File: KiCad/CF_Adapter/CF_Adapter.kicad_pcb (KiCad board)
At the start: 2 copper layers, 38.1 x 53.3 mm, 3 parts, among them J1 Z-Fighter IDE Connector, J2 CF Card Socket

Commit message: Silkscreen, Gerber settings
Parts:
- added G***: LOGO, Z-Fighter:Tangent_Head, B.Cu at (150.9, 117.5)

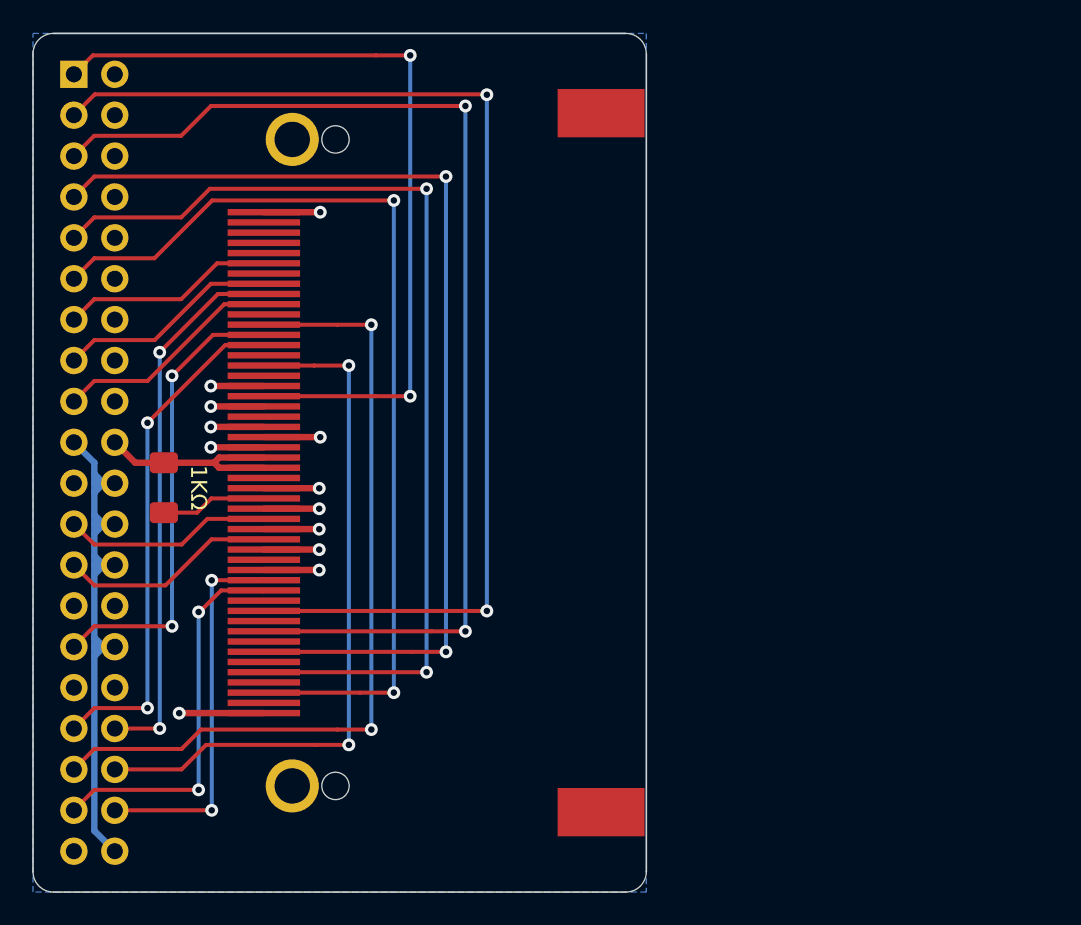
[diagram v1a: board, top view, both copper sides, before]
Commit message: Fixed copper pours
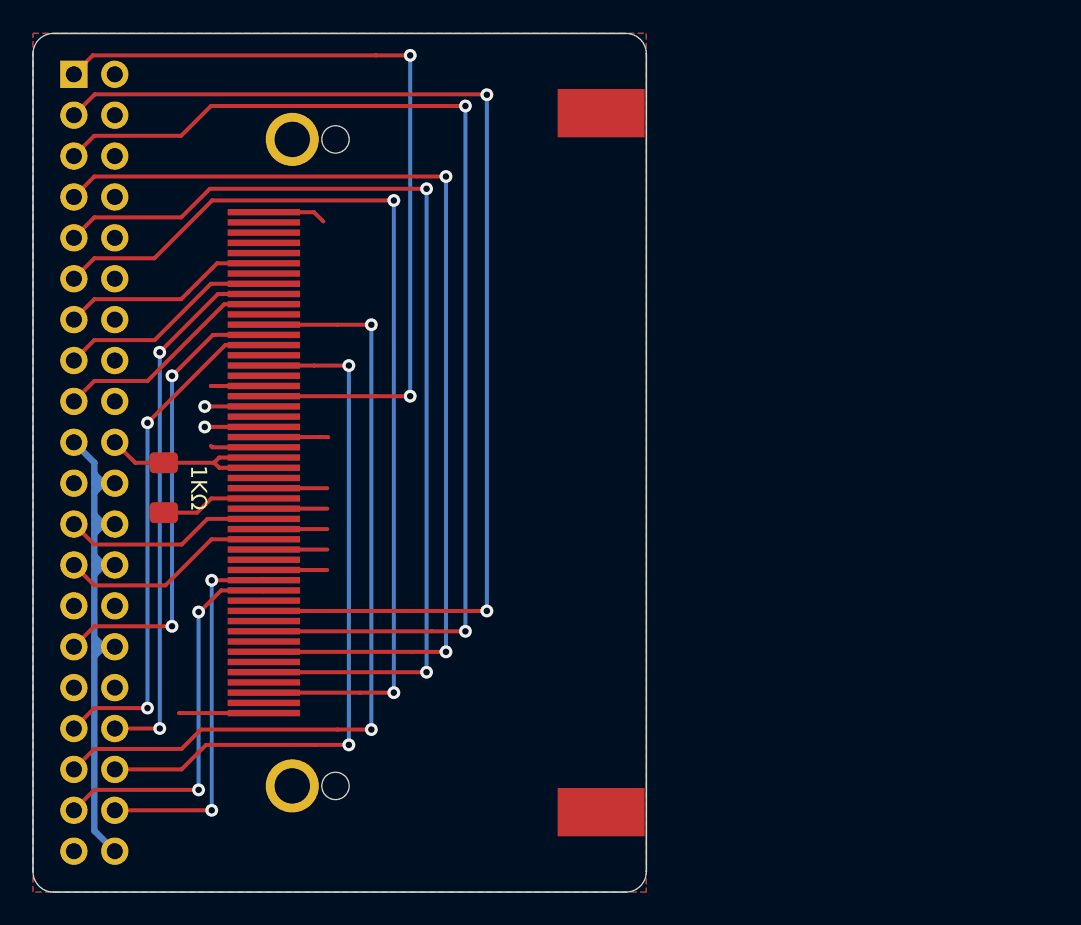
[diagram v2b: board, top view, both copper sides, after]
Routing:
- net GND: track 82.2 -> 82.6 mm, vias 12 -> 2
- added copper zone on F.Cu, net GND

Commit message: Redesigned CF adapter for low-profile socket
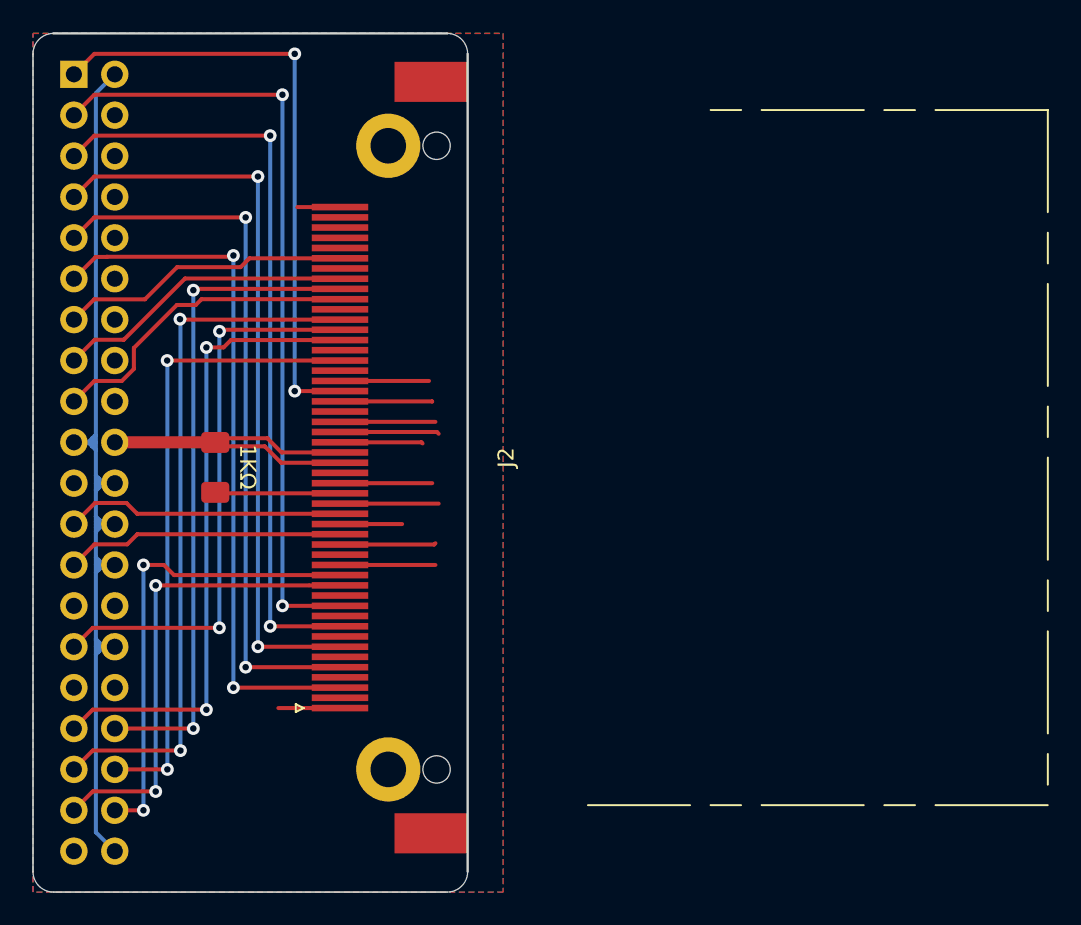
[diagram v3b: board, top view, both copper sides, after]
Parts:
- removed G***: LOGO, Z-Fighter:Tangent_Head
- J2: value CF Card Socket -> Conn_02x25_Top_Bottom; footprint Connector_Card:315610050210871 -> Connector_Card:CF-Card_3M_N7E50-7516PK-20-WF
- moved R1 3.43 mm to (133.2, 98.7)
- moved J2 1.51 mm to (150.4, 98.1), turned to 270 degrees
- renumbered 1KΩ to R1
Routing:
- net GND: track 82.6 -> 131.8 mm, vias 2 -> 0
- net D6: track 71.0 -> 47.6 mm
- net D7: track 72.1 -> 49.2 mm
- net D4: track 63.2 -> 44.7 mm
- net D5: track 64.4 -> 45.9 mm
- net D3: track 60.4 -> 44.0 mm
- net #RESET: track 51.6 -> 37.9 mm
- net VCC: track 13.1 -> 22.9 mm
- net A1: track 32.0 -> 39.8 mm
- net A0: track 51.3 -> 43.9 mm
- net PATA34: track 34.1 -> 41.4 mm
- net PATA29: track 29.0 -> 35.4 mm
- net PATA38: track 23.6 -> 29.5 mm
- net D0: track 14.3 -> 19.9 mm
- net D1: track 13.8 -> 18.6 mm
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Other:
- board size 38.1 x 53.3 mm -> 27 x 53.3 mm
- board text added: "Z-Fighter CF Adapter Rev. 1 @tangent3D 2021"
- board text removed: "Z-Fighter CF Adapter Rev. 0 @tangent3D 2021"

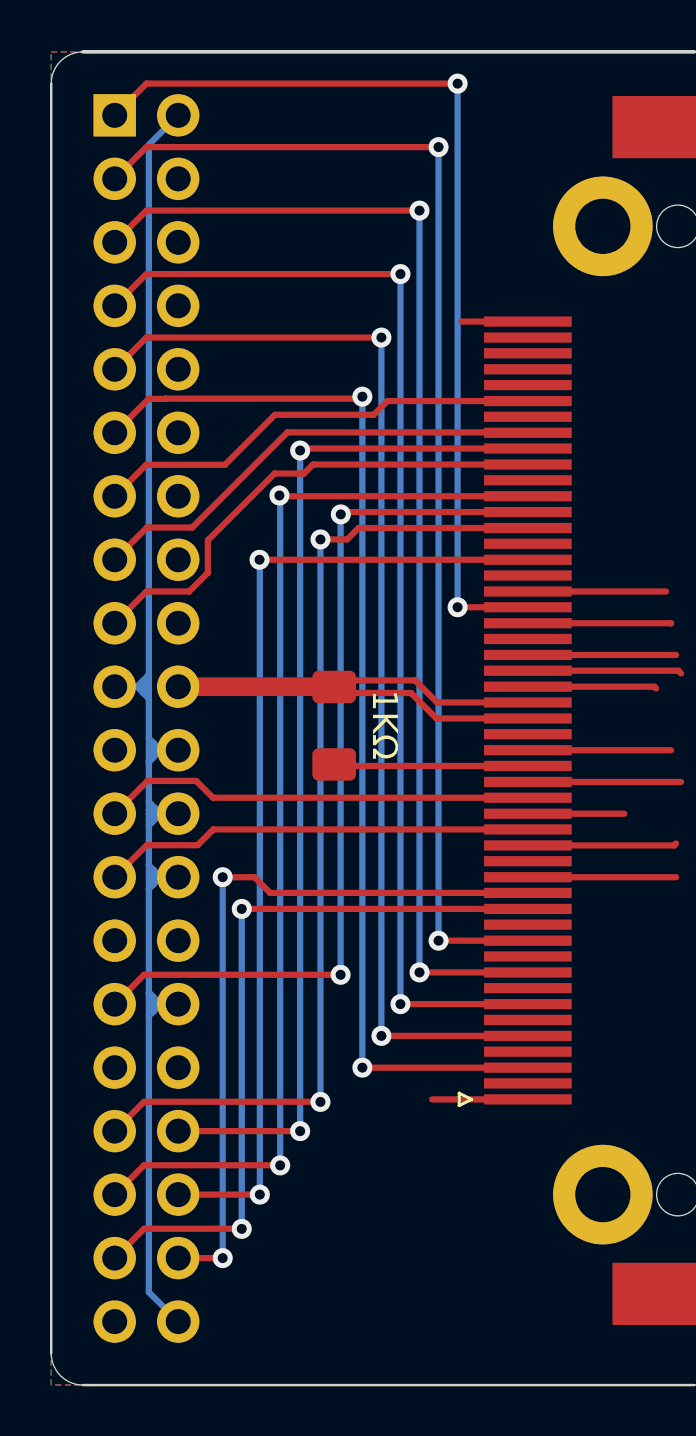
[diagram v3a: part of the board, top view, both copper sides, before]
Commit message: Update CF_Adapter.kicad_pcb
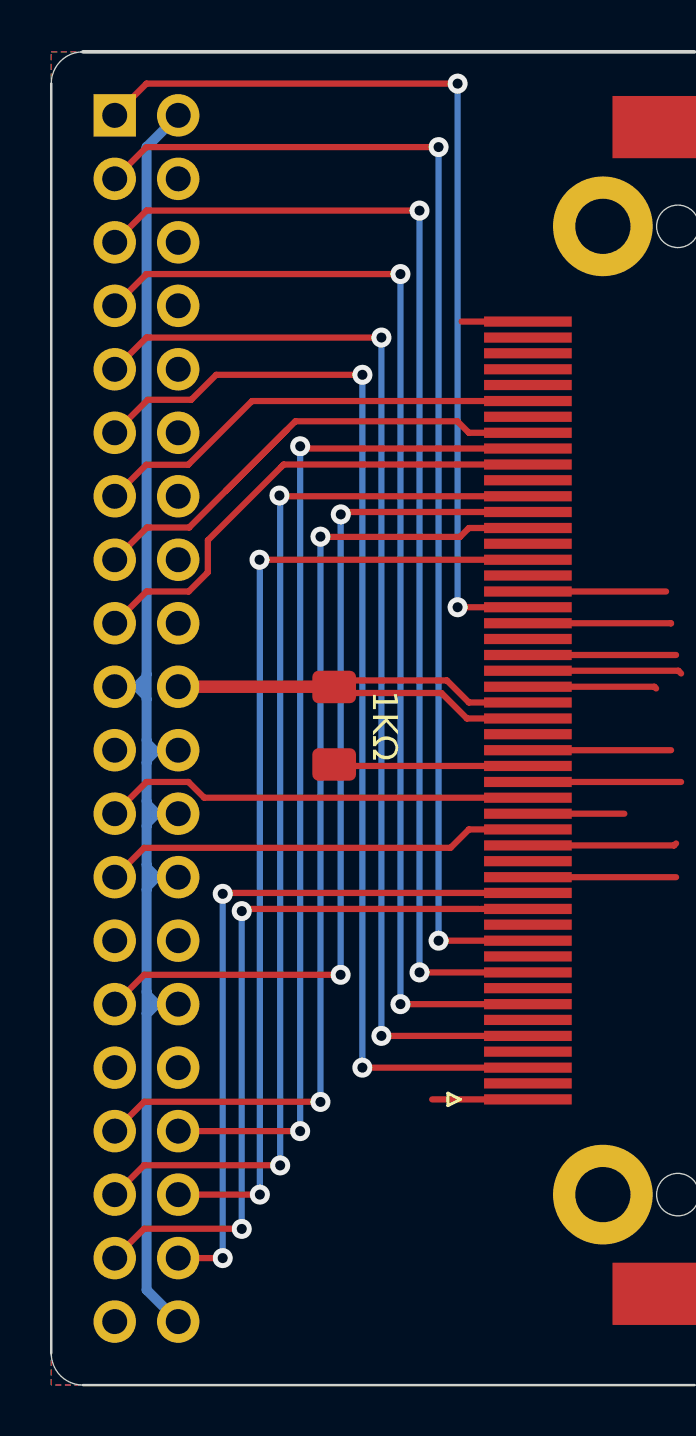
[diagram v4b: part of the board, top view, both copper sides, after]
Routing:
- net D1: track 18.6 -> 22.4 mm
- net D3: track 44.0 -> 45.1 mm
- net PATA38: track 29.5 -> 28.6 mm

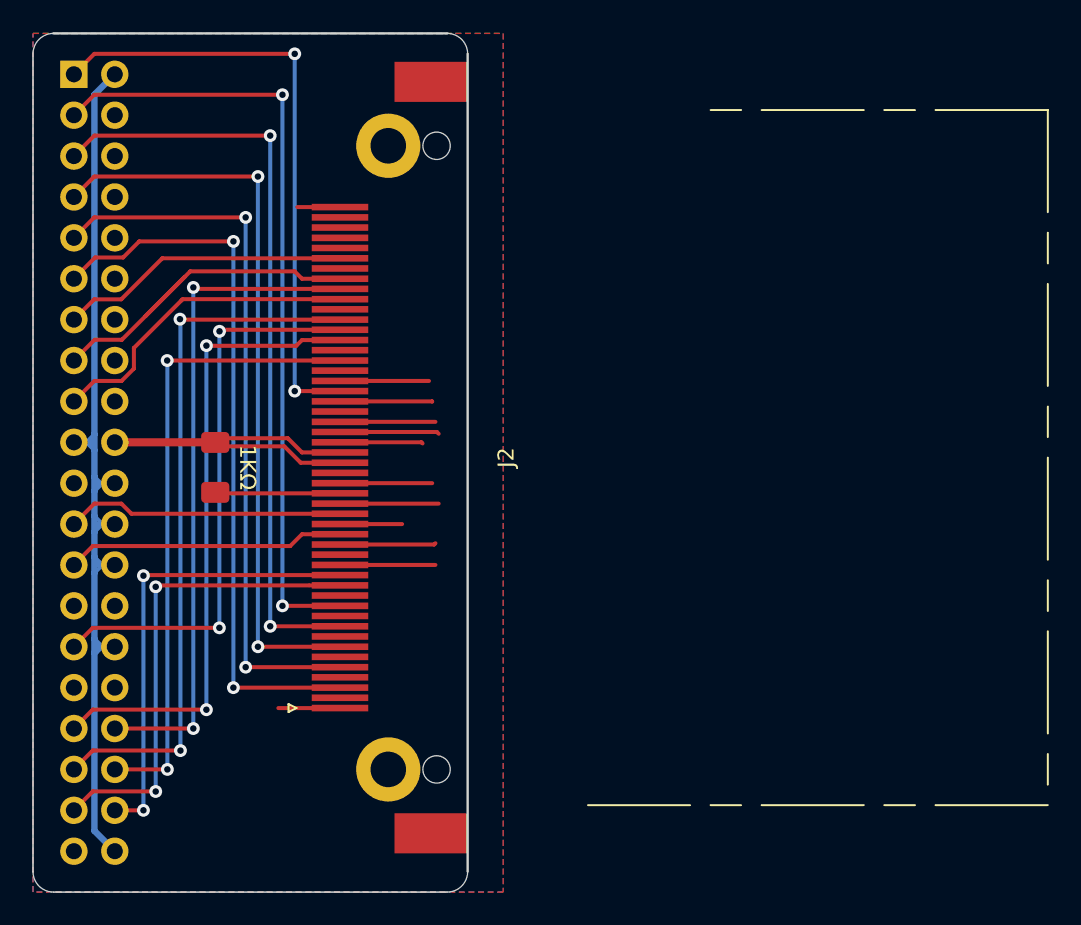
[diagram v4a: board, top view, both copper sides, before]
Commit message: Update CF_Adapter.kicad_pcb
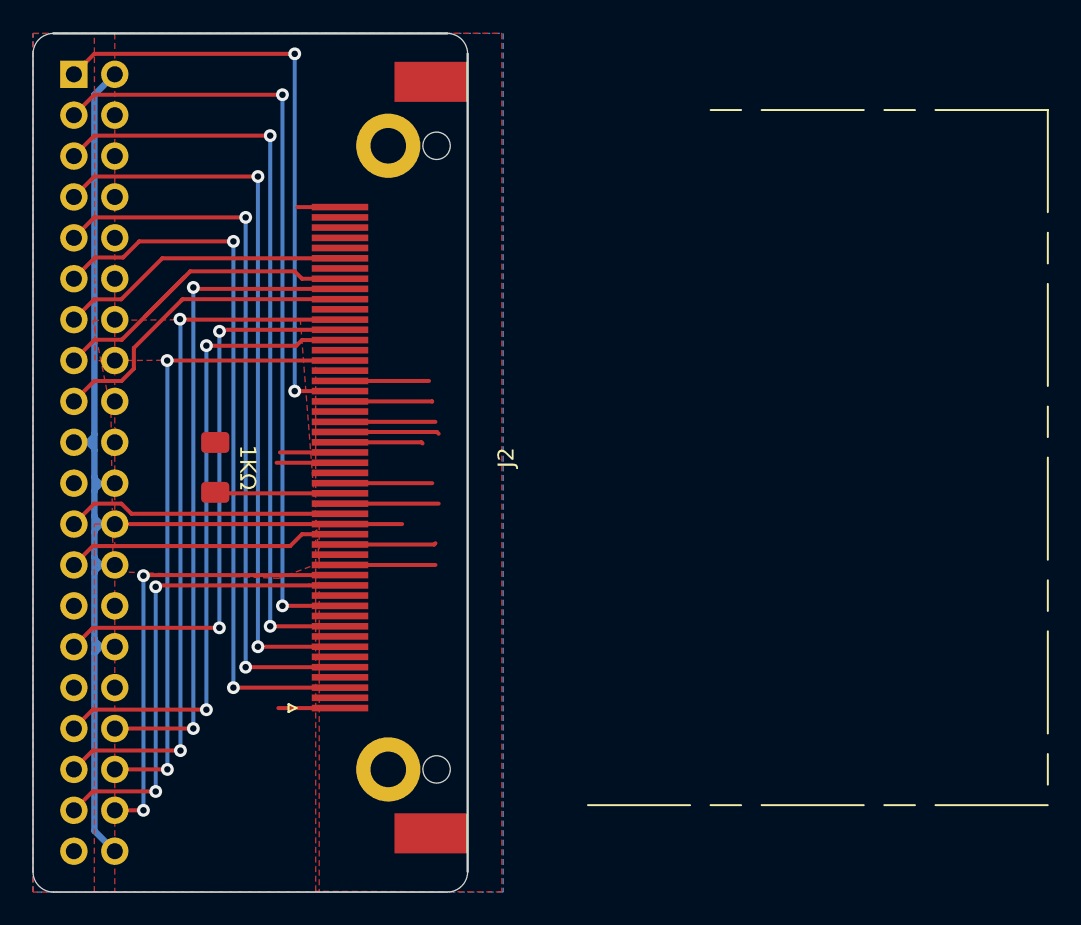
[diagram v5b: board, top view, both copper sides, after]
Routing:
- net VCC: track 22.9 -> 8.49 mm
- net GND: track 131.4 -> 145.4 mm
- added copper zone on F.Cu, net VCC
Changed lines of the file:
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@@
     (thickness 1.6)
     (drawings 9)
-    (tracks 189)
+    (tracks 185)
     (zones 0)
     (modules 3)
@@
       (effects (font (size 1 1) (thickness 0.15)))
     )
-    (fp_text user %R (at 0 5.815 270) (layer F.Fab)
-      (effects (font (size 1 1) (thickness 0.15)))
-    )
     (fp_line (start 15.31 12.65) (end 15.56 12.15) (layer F.SilkS) (width 0.12))
     (fp_line (start 15.81 12.65) (end 15.31 12.65) (layer F.SilkS) (width 0.12))
@@
     (fp_line (start -0.64 4.21) (end 0.64 2.94) (layer F.Fab) (width 0.1))
     (fp_line (start -24.84 11.45) (end 24.84 11.45) (layer F.CrtYd) (width 0.05))
+    (fp_text user %R (at 0 5.815 270) (layer F.Fab)
+      (effects (font (size 1 1) (thickness 0.15)))
+    )
     (pad 1 smd rect (at 15.56 9.45 90) (size 0.41 3.51) (layers F.Cu F.Paste F.Mask)
       (net 2 GND))
@@
   (gr_line (start 121.84 123.78) (end 121.84 72.98) (layer Edge.Cuts) (width 0.1))
   (gr_line (start 147.569999 125.05) (end 123.11 125.05) (layer Edge.Cuts) (width 0.1))
+  (via (at 138.098 93.93) (size 0.8) (drill 0.4) (layers F.Cu B.Cu) (net 1))
+  (segment (start 140.84 93.93) (end 138.098 93.93) (width 0.25) (layer F.Cu) (net 1) (status 10))
   (via (at 138.098 72.98) (size 0.8) (drill 0.4) (layers F.Cu B.Cu) (net 1))
-  (via (at 138.098 93.93) (size 0.8) (drill 0.4) (layers F.Cu B.Cu) (net 1))
   (segment (start 138.098 72.98) (end 138.098 93.93) (width 0.25) (layer B.Cu) (net 1))
-  (segment (start 140.84 93.93) (end 138.098 93.93) (width 0.25) (layer F.Cu) (net 1) (status 10))
   (segment (start 125.65 72.98) (end 124.38 74.25) (width 0.25) (layer F.Cu) (net 1) (status 20))
   (segment (start 138.098 72.98) (end 125.65 72.98) (width 0.25) (layer F.Cu) (net 1))
@@
   (segment (start 125.65508 109.3147) (end 125.65508 110.18084) (width 0.4) (layer B.Cu) (net 2))
   (segment (start 125.65508 110.18084) (end 125.65508 121.24508) (width 0.4) (layer B.Cu) (net 2))
+  (segment (start 140.91 102.19) (end 126.92 102.19) (width 0.25) (layer F.Cu) (net 2))
   (via (at 137.336 75.52) (size 0.8) (drill 0.4) (layers F.Cu B.Cu) (net 3))
   (segment (start 137.405001 75.614999) (end 137.5 75.52) (width 0.25) (layer F.Cu) (net 3))
@@
   (segment (start 133.07 97.11) (end 133.14 97.18) (width 0.25) (layer F.Cu) (net 19) (status 30))
   (segment (start 133.15 97.11) (end 133.16 97.12) (width 0.5) (layer F.Cu) (net 19) (status 30))
-  (segment (start 126.92 97.11) (end 133.15 97.11) (width 0.5) (layer F.Cu) (net 19) (status 30))
   (segment (start 133.46146 96.85854) (end 133.14 97.18) (width 0.25) (layer F.Cu) (net 19))
-  (segment (start 137.66854 96.85854) (end 133.46146 96.85854) (width 0.25) (layer F.Cu) (net 19))
-  (segment (start 138.55 97.74) (end 137.66854 96.85854) (width 0.25) (layer F.Cu) (net 19))
-  (segment (start 140.91 97.74) (end 138.55 97.74) (width 0.25) (layer F.Cu) (net 19))
-  (segment (start 140.91 98.38) (end 138.47 98.38) (width 0.25) (layer F.Cu) (net 19) (status 10))
-  (segment (start 138.47 98.38) (end 137.45146 97.36146) (width 0.25) (layer F.Cu) (net 19))
-  (segment (start 137.45146 97.36146) (end 133.32146 97.36146) (width 0.25) (layer F.Cu) (net 19) (status 20))
   (segment (start 133.32146 97.36146) (end 133.14 97.18) (width 0.25) (layer F.Cu) (net 19) (status 30))
+  (segment (start 140.91 97.74) (end 137.18 97.74) (width 0.25) (layer F.Cu) (net 19))
+  (segment (start 140.91 98.38) (end 136.97 98.38) (width 0.25) (layer F.Cu) (net 19))
   (segment (start 127.96 101.55) (end 140.91 101.55) (width 0.25) (layer F.Cu) (net 21))
   (segment (start 127.33 100.92) (end 127.96 101.55) (width 0.25) (layer F.Cu) (net 21))
@@
     (polygon
       (pts
-        (xy 151.05 125.05) (xy 121.84 125.05) (xy 121.84 71.71) (xy 151.05 71.71)
+        (xy 126.92 125.05) (xy 121.84 125.05) (xy 121.84 71.71) (xy 126.92 71.71)
       )
     )
@@
     )
   )
-  (zone (net 0) (net_name "") (layer F.Cu) (hatch edge 0.508)
+  (zone (net 19) (net_name VCC) (layer F.Cu) (hatch edge 0.508)
     (connect_pads (clearance 0.48))
     (min_thickness 0.254)
-    (keepout (tracks allowed) (vias allowed) (copperpour not_allowed))
-    (fill (arc_segments 32) (thermal_gap 0.508) (thermal_bridge_width 0.508))
+    (fill yes (arc_segments 32) (thermal_gap 0.508) (thermal_bridge_width 0.508))
     (polygon
       (pts
-        (xy 137.334 96.221) (xy 138.096 101.047) (xy 131.238 103.206) (xy 127.047 103.333) (xy 126.793 97.11)
-        (xy 126.666 97.11) (xy 128.444 94.951)
+        (xy 139.63 104.62) (xy 137.1 105.56) (xy 126.82 105.14) (xy 126.67 94.37) (xy 126.55 94.49)
+        (xy 125.56 89.54) (xy 138.44 89.44)
       )
     )
+  )
+  (zone (net 2) (net_name GND) (layer F.Cu) (hatch edge 0.508)
+    (connect_pads (clearance 0.48))
+    (min_thickness 0.254)
+    (fill yes (arc_segments 32) (thermal_gap 0.508) (thermal_bridge_width 0.508))
+    (polygon
+      (pts
+        (xy 150.96 125.04) (xy 139.4 125.002096) (xy 139.4 91.977905) (xy 125.695 92.035) (xy 125.65 71.71)
+        (xy 140.8 71.7) (xy 140.80002 71.708959) (xy 150.96 71.7)
+      )
+    )
+  )
+  (zone (net 2) (net_name GND) (layer F.Cu) (hatch edge 0.508)
+    (connect_pads (clearance 0.48))
+    (min_thickness 0.254)
+    (fill yes (arc_segments 32) (thermal_gap 0.508) (thermal_bridge_width 0.508))
+    (polygon
+      (pts
+        (xy 139.62 125.05) (xy 125.65 125.05) (xy 125.65 102.19) (xy 139.62 102.19)
+      )
+    )
